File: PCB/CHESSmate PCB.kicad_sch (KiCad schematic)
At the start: 51 parts, among them J1 Conn_01x22_Pin, Q1 2N2222, Q2 2N2222, Q3 2N2222, Q4 2N2222, SW1 A, SW10 2, SW11 3, SW12 4, SW13 5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

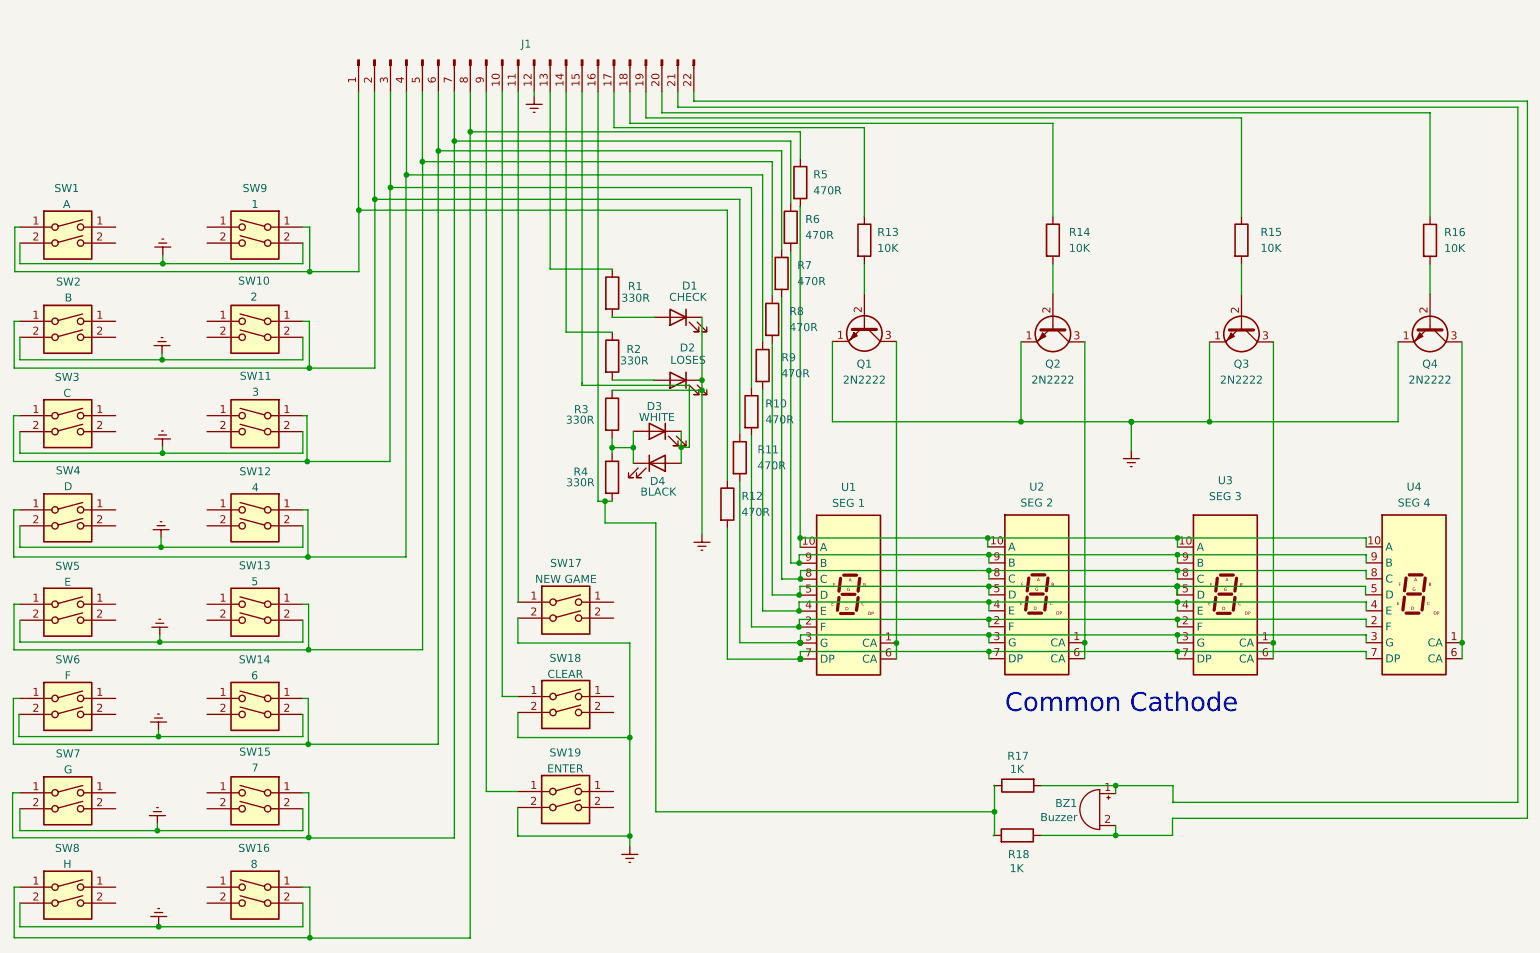
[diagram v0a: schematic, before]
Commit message: 23 pin CPU connector
This doesn't work because you can't use GPIO6, so I designed a new CPU board with a Pi Pico
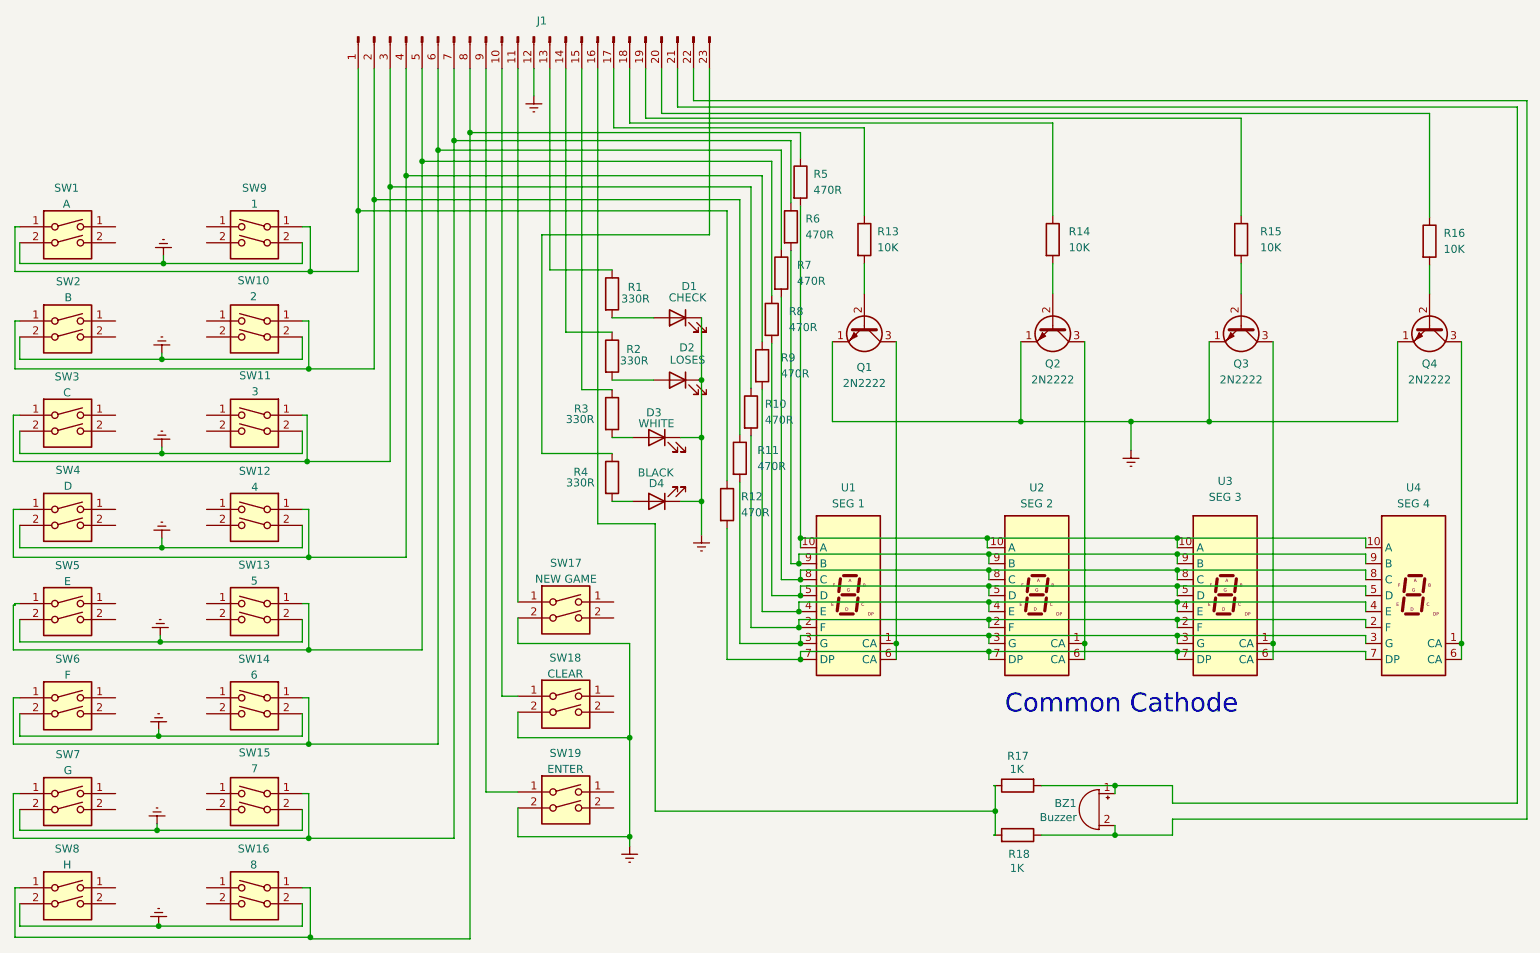
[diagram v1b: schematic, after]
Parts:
- J1: value Conn_01x22_Pin -> ~; footprint (none) -> Connector_PinHeader_2.54mm:PinHeader_1x23_P2.54mm_Vertical; symbol Connector:Conn_01x22_Pin -> Connector:Conn_01x23_Pin
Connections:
- net GNDREF: now also D3.1 (K), D4.1 (K); no longer R3.1
- net at D3.2 (A), R3.2: no longer D4.1 (K), R4.1
- net at SW11.1: now also J1.3 (Pin_3), R10.1, SW3.1
- net at SW17.1: now also J1.11 (Pin_11)
- net at SW9.1: now also J1.1 (Pin_1), R12.1, SW1.1
- net at J1.16 (Pin_16), R17.1, R18.2: no longer R4.2
- net at SW18.1: now also J1.10 (Pin_10)
- net at SW14.1: now also J1.6 (Pin_6), R7.1, SW6.1
- net at SW19.1: now also J1.9 (Pin_9)
- net at SW8.1: now also J1.8 (Pin_8), R5.1, SW16.1
- net at SW7.1: now also J1.7 (Pin_7), R6.1, SW15.1
- new net: D4.2 (A), R4.2
- new net: J1.15 (Pin_15), R3.1
- new net: J1.23 (Pin_23), R4.1
- now unconnected: SW1.1, SW15.1, SW16.1, SW3.1, SW6.1
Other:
- moved on the sheet: D3, D4
